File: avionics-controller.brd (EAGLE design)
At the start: 50.8 x 50.8 mm, 52 parts, among them U1 SN65HVD10_D_8, Y1 ABS25-32.768KHZ

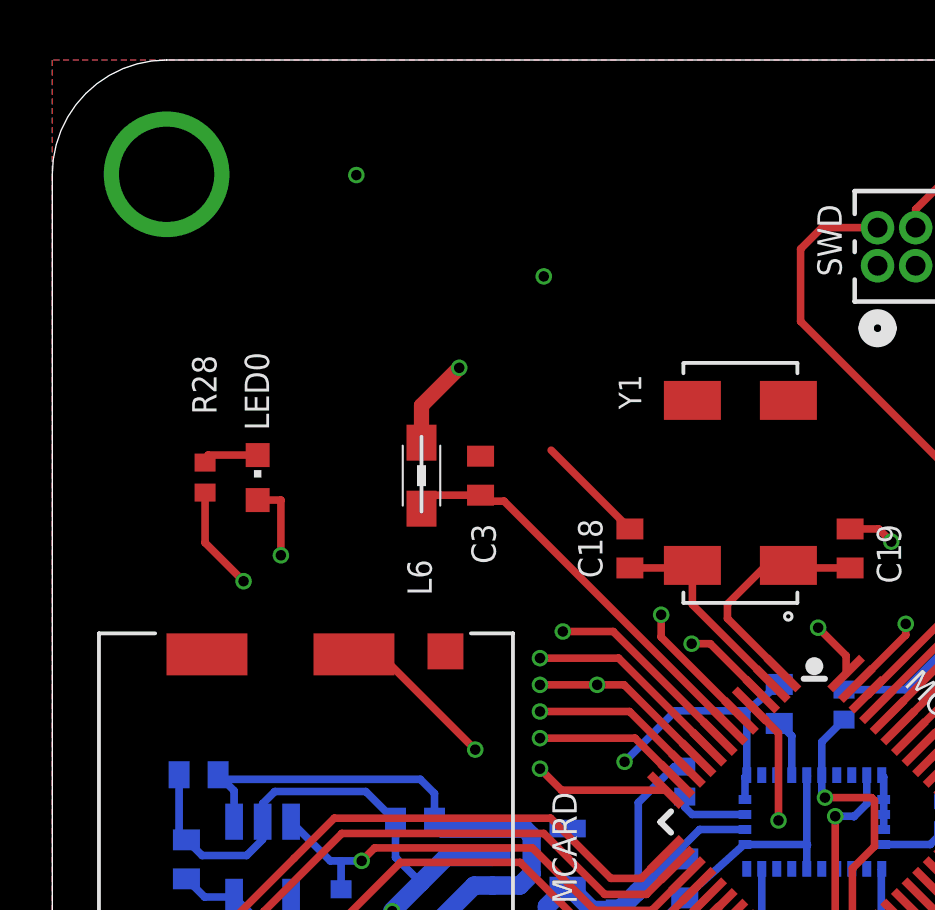
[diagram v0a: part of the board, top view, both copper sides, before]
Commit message: Updated documentation(pinout, bom) and made small layout adjustment
Added another BOM, updated BOM readme to remove markdown table and replaced with links, fixed small layout error that caused sd card to short GND to filters 5V pad when fully open. Added more datasheets.
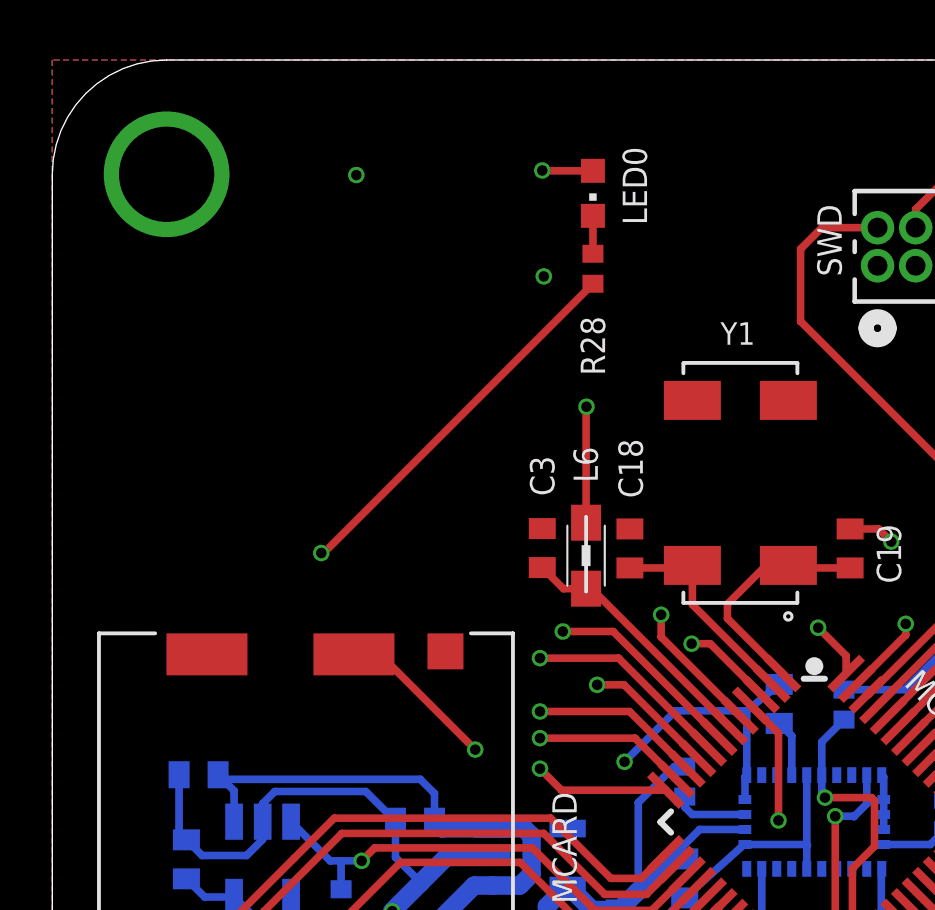
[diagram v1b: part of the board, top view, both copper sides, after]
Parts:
- moved R28 14.7 mm to (18.0, 43.8)
- moved LED0 14.7 mm to (18.0, 46.4), turned to 180 degrees
- moved L6 6.10 mm to (17.8, 34.3)
- moved C3 3.17 mm to (16.3, 34.5)
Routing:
- net LED0: track 31.5 -> 40.6 mm
- net N$2: track 13.6 -> 8.72 mm
- net PA04/AIN4: track 38.8 -> 35.0 mm, vias 2 -> 1
- net GND: track 162.7 -> 159.0 mm
- net 3.3V: track 68.6 -> 67.7 mm
- net 5V: track 97.4 -> 98.3 mm
- net N$20: track 1.92 -> 1.26 mm
